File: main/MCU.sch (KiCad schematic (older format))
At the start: 23 parts, among them J4 BACKUP_SPI_OUT, J5 MCU_debug, J6 MCU_GPIO, U4 EFM32GG12B810F1024GQ64, Y1 48MHz

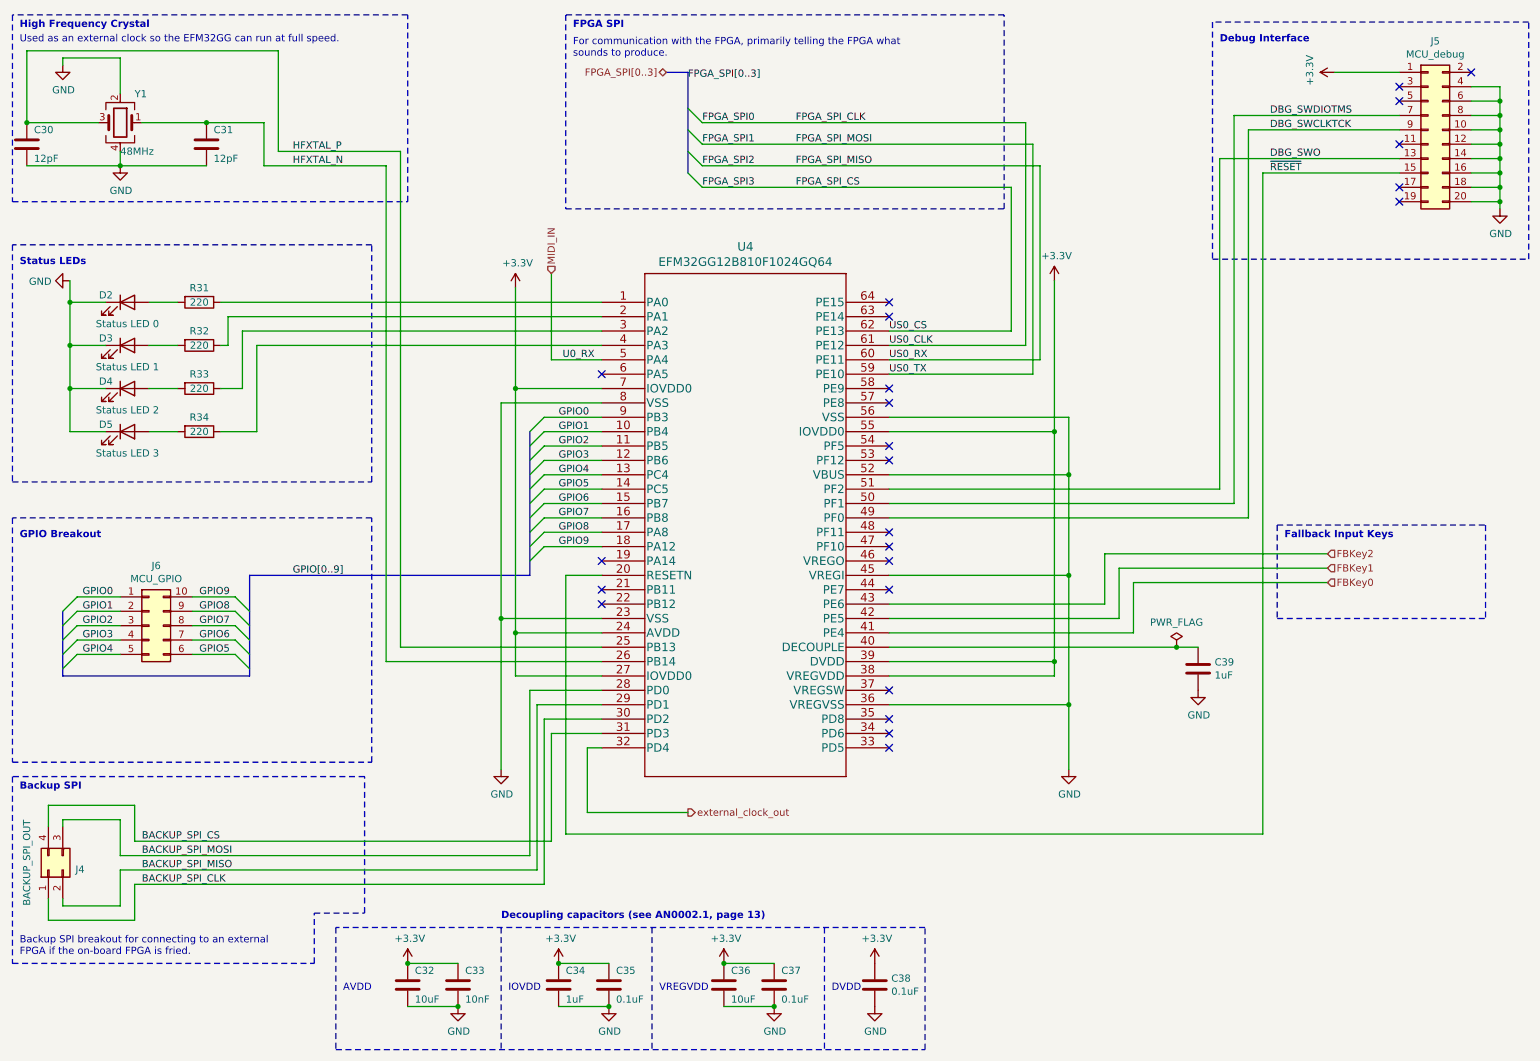
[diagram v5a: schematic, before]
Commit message: Add FPGA RAM chip
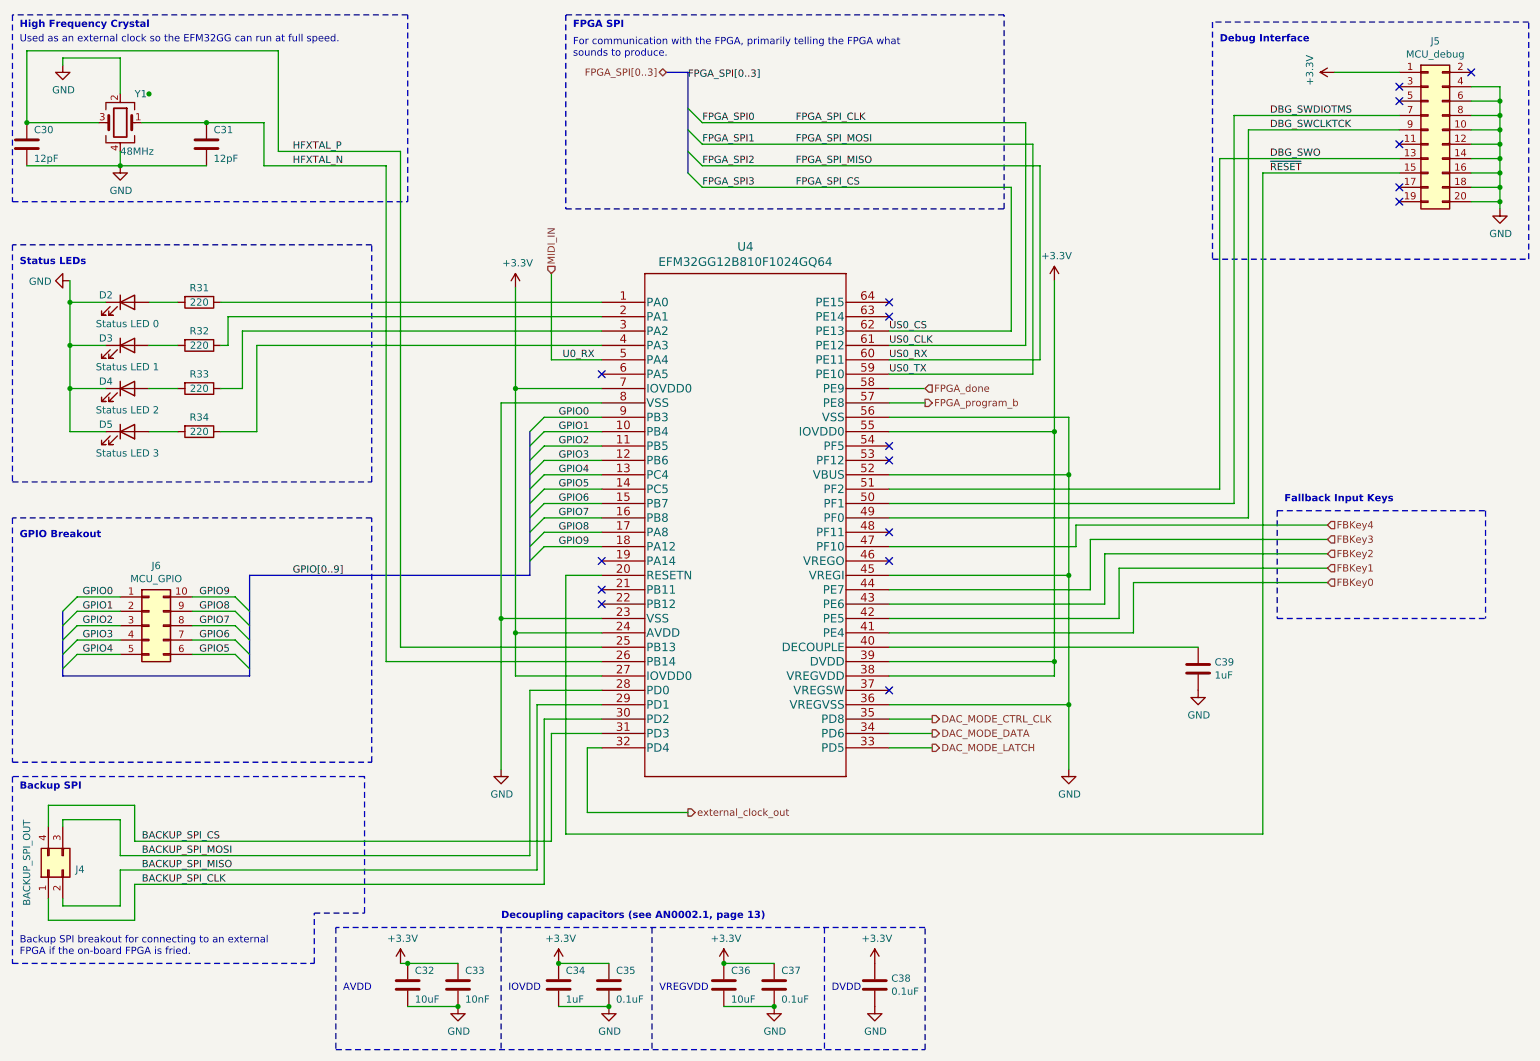
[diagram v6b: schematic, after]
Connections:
- net DAC_MODE_LATCH: now reaches U4.33 (PD5)
- net DAC_MODE_DATA: now reaches U4.34 (PD6)
- net DAC_MODE_CTRL_CLK: now reaches U4.35 (PD8)
- net FBKey3: now reaches U4.44 (PE7)
- net FBKey4: now reaches U4.47 (PF10)
- net FPGA_program_b: now reaches U4.57 (PE8)
- net FPGA_done: now reaches U4.58 (PE9)
- no-connect marks 24 -> 17
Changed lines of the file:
@@
 $Descr A4 11693 8268
 encoding utf-8
-Sheet 3 7
+Sheet 7 7
 Title "MIDI Audio Box"
 Date "2021-09-21"
@@
 	1    0    0    -1
 $EndComp
-Wire Wire Line
-	8650 4950 8800 4950
-Connection ~ 8650 4950
-$Comp
-L power:PWR_FLAG #FLG0101
-U 1 1 6152DFA6
-P 8650 4950
-F 0 "#FLG0101" H 8650 5025 50  0001 C CNN
-F 1 "PWR_FLAG" H 8650 5123 50  0000 C CNN
-F 2 "" H 8650 4950 50  0001 C CNN
-F 3 "~" H 8650 4950 50  0001 C CNN
-	1    8650 4950
-	1    0    0    -1
-$EndComp
-Wire Wire Line
-	6650 4950 8650 4950
 $Comp
 L Device:C C32
@@
 L power:+3.3V #PWR0142
 U 1 1 6158214A
-P 3300 7150
-F 0 "#PWR0142" H 3300 7000 50  0001 C CNN
-F 1 "+3.3V" H 3315 7323 50  0000 C CNN
-F 2 "" H 3300 7150 50  0001 C CNN
-F 3 "" H 3300 7150 50  0001 C CNN
-	1    3300 7150
+P 3250 7150
+F 0 "#PWR0142" H 3250 7000 50  0001 C CNN
+F 1 "+3.3V" H 3265 7323 50  0000 C CNN
+F 2 "" H 3250 7150 50  0001 C CNN
+F 3 "" H 3250 7150 50  0001 C CNN
+	1    3250 7150
 	1    0    0    -1
 $EndComp
@@
 NoConn ~ 4650 4550
 NoConn ~ 4650 4650
-NoConn ~ 6650 5650
-NoConn ~ 6650 5450
 NoConn ~ 6650 5250
-NoConn ~ 6650 4550
-NoConn ~ 6650 4250
 NoConn ~ 6650 4150
 NoConn ~ 6650 3650
 NoConn ~ 6650 3550
-NoConn ~ 6650 3250
-NoConn ~ 6650 3150
 NoConn ~ 6650 2650
 NoConn ~ 6650 2550
@@
 Wire Wire Line
 	4150 5250 4150 6400
-NoConn ~ 6650 5550
 Wire Wire Line
 	4650 5150 4050 5150
@@
 Debug Interface
 Wire Notes Line
-	9350 4100 9350 4750
+	9350 4000 9350 4750
 Wire Notes Line
 	9350 4750 10800 4750
 Wire Notes Line
-	9350 4100 10800 4100
-Wire Notes Line
-	10800 4100 10800 4750
-Text Notes 9400 4200 0    50   ~ 10
+	9350 4000 10800 4000
+Wire Notes Line
+	10800 4000 10800 4750
+Text Notes 9400 3950 0    50   ~ 10
 Fallback Input Keys
 Wire Notes Line
@@
 Wire Wire Line
 	4550 6100 5250 6100
+Text HLabel 5250 6100 2    50   Output ~ 0
+external_clock_out
+Text HLabel 6900 3150 2    50   Input ~ 0
+FPGA_done
+Wire Wire Line
+	6650 3150 6900 3150
+Text HLabel 6900 3250 2    50   Output ~ 0
+FPGA_program_b
+Wire Wire Line
+	6650 3250 6900 3250
+Text HLabel 6950 5450 2    50   Output ~ 0
+DAC_MODE_CTRL_CLK
+Text HLabel 6950 5550 2    50   Output ~ 0
+DAC_MODE_DATA
+Text HLabel 6950 5650 2    50   Output ~ 0
+DAC_MODE_LATCH
+Wire Wire Line
+	6950 5450 6650 5450
+Wire Wire Line
+	6950 5550 6650 5550
+Wire Wire Line
+	6650 5650 6950 5650
+Wire Wire Line
+	3250 7150 3300 7150
+Wire Wire Line
+	6650 4950 8800 4950
+Wire Wire Line
+	8050 4550 8050 4200
+Wire Wire Line
+	8050 4200 9700 4200
+Text HLabel 9700 4200 2    50   Input ~ 0
+FBKey3
+Text HLabel 9700 4100 2    50   Input ~ 0
+FBKey4
+Wire Wire Line
+	6650 4250 7950 4250
+Wire Wire Line
+	7950 4250 7950 4100
+Wire Wire Line
+	7950 4100 9700 4100
+Wire Wire Line
+	6650 4550 8050 4550
 Wire Bus Line
 	5250 950  5250 1650
@@
 Wire Bus Line
 	4150 3450 4150 4450
-Text HLabel 5250 6100 2    50   Output ~ 0
-external_clock_out
+Connection ~ 1500 1100
 $EndSCHEMATC

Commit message: Final cleanup before sending in for rebiew
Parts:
- renumbered C30 to C57, C31 to C58, C32 to C59, C33 to C60, C34 to C61, C35 to C62, C36 to C63, C37 to C64, C38 to C65, C39 to C66, D2 to D3, D3 to D4, D4 to D5, D5 to D6, J4 to J10, J6 to J11, J5 to J12, R31 to R40, R32 to R41, R33 to R42, R34 to R43, U4 to U5

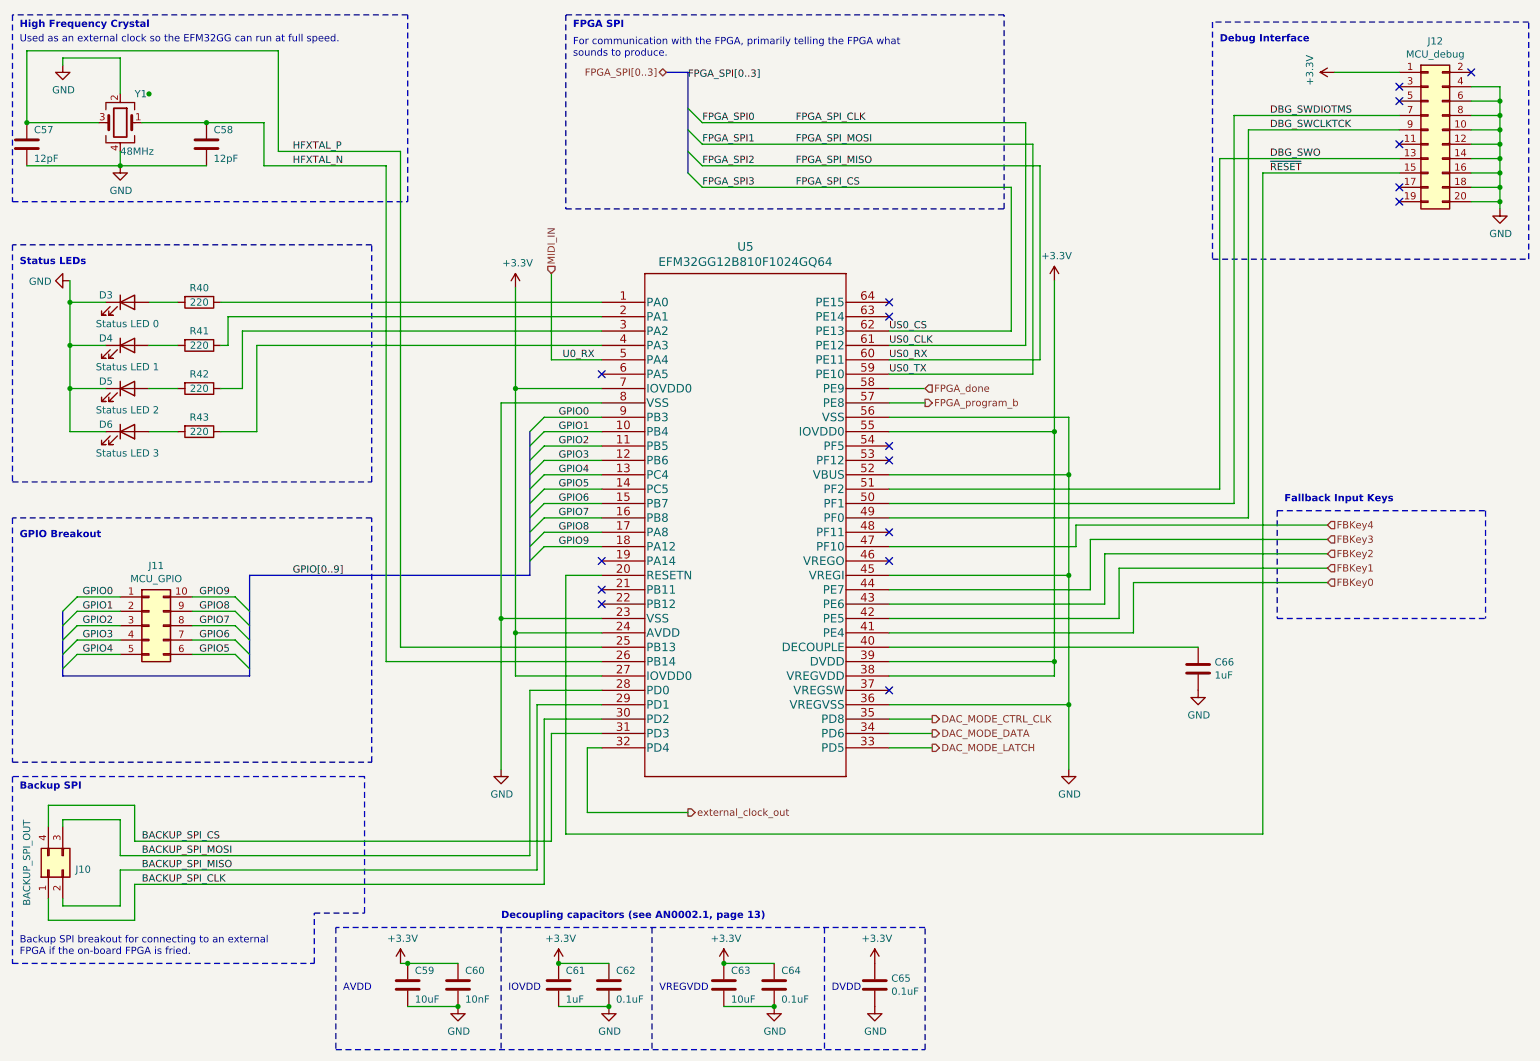
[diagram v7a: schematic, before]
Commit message: Fix up after review
Done:
- Add bulk decoupling capacitor to switch regulator cirucit
- Disconnect DONE from PROGRAM_B in FPGA (mistake)
- The decoupling capacitors used for the FPGA were for the 15T, not the
  100T. It was also setup for two I/O banks, we only use one. Disconnect
  I/O bank 15.
- Switch external clock on the MCU to an oscillator, allowing for 72MHz
- Switch pinout of the backup SPI on the MCU so that half the pins are
  ground

Mizzing:
- Add low-pass filters to the output of the DAC as per the datasheet.
  May remove the need for the amplifier circuit.
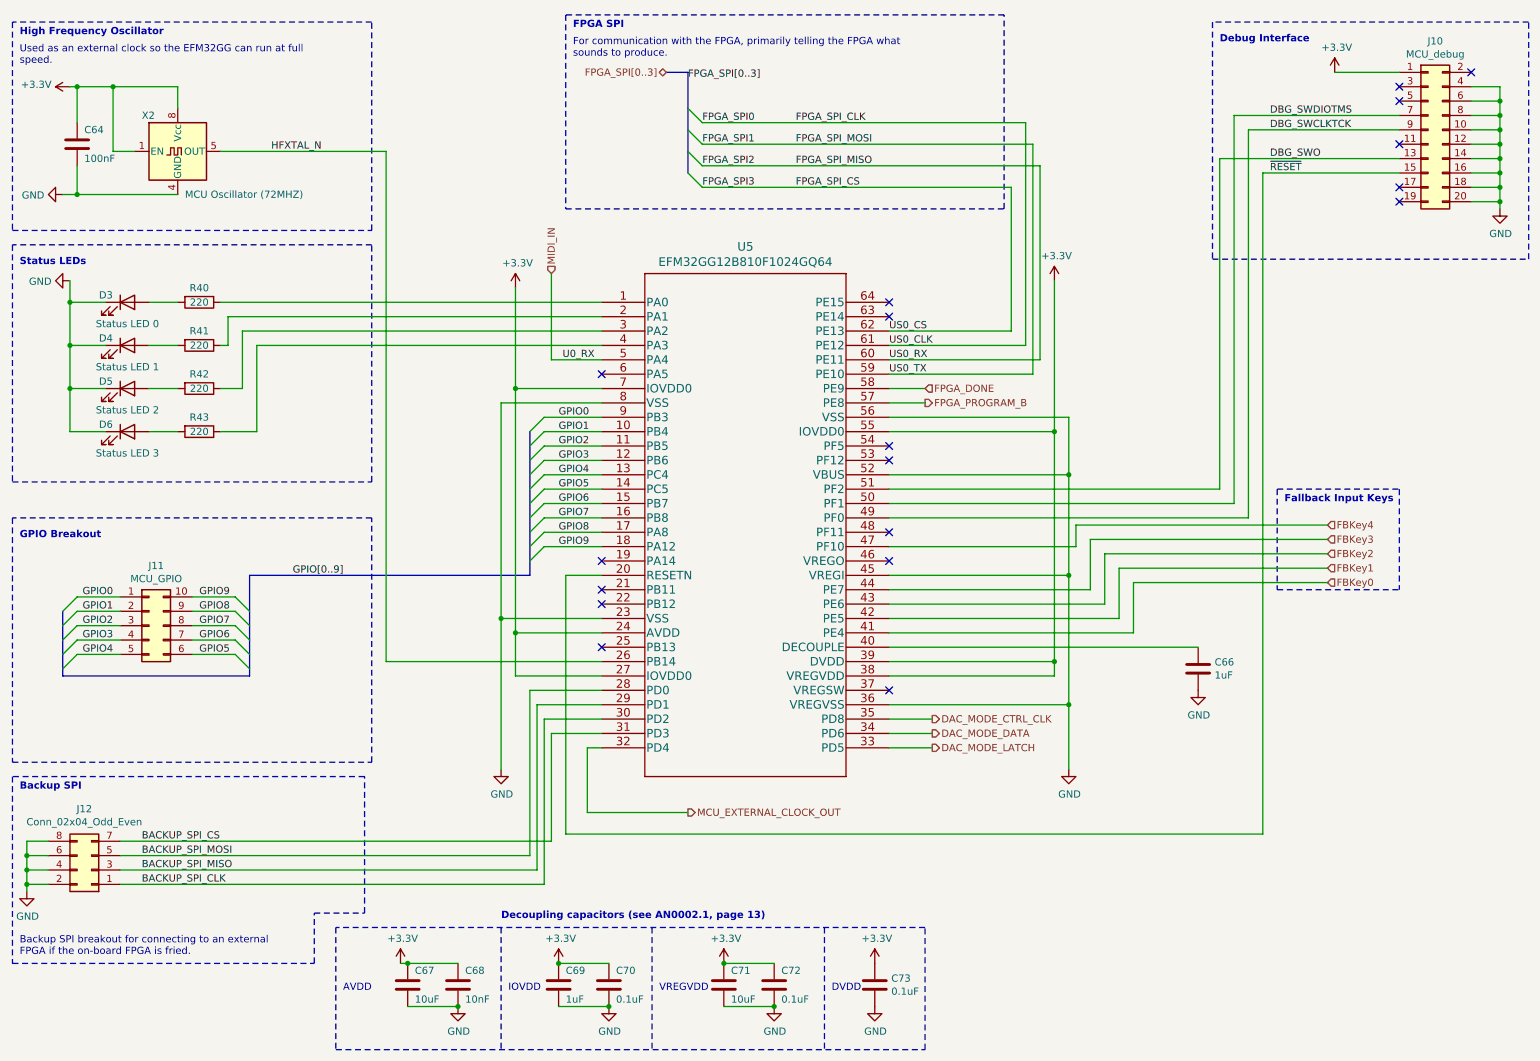
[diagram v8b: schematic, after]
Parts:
- removed C57, C58: 12pF, symbol Device:C
- removed J10: BACKUP_SPI_OUT, symbol Connector_Generic:Conn_02x02_Counter_Clockwise
- removed Y1: 48MHz, symbol Device:Crystal_GND24
- added C64: 100nF, symbol Device:C
- added J12: Conn_02x04_Odd_Even, symbol Connector_Generic:Conn_02x04_Odd_Even
- added X2: MCU Oscillator (72MHZ), Oscillator:Oscillator_DIP-8, symbol Oscillator:CXO_DIP8
- D3, D4, D5, D6: footprint (none) -> LED_SMD:LED_0805_2012Metric_Pad1.15x1.40mm_HandSolder
- R40, R41, R42, R43: footprint (none) -> Resistor_SMD:R_0805_2012Metric_Pad1.20x1.40mm_HandSolder
- renumbered C59 to C67, C60 to C68, C61 to C69, C62 to C70, C63 to C71, C64 to C72, C65 to C73, J12 to J10
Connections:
- net +3V3: now also C64.1, X2.1 (EN), X2.8 (Vcc)
- net BACKUP_SPI_CLK: now also J12.1 (Pin_1)
- net BACKUP_SPI_CS: now also J12.7 (Pin_7)
- net BACKUP_SPI_MISO: now also J12.3 (Pin_3)
- net BACKUP_SPI_MOSI: now also J12.5 (Pin_5)
- net GND: now also C64.2, J12.2 (Pin_2), J12.4 (Pin_4), J12.6 (Pin_6), J12.8 (Pin_8), X2.4 (GND)
- net HFXTAL_N: now also X2.5 (OUT)
- net FPGA_done renamed FPGA_DONE
- net FPGA_program_b renamed FPGA_PROGRAM_B
- net HFXTAL_P: no longer names the net of U5.25 (PB13)
- net external_clock_out renamed MCU_EXTERNAL_CLOCK_OUT
- no-connect marks 17 -> 18
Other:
- note added: "High Frequency Oscillator"
- note added: "Used as an external clock so the EFM32GG can run at full\nspeed."
- note removed: "High Frequency Crystal"
- note removed: "Used as an external clock so the EFM32GG can run at full speed."
